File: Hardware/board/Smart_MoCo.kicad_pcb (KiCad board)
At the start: 4 copper layers, 26.9 x 39.9 mm, 37 parts, among them J1 Conn_01x02, J2 Conn_01x04, J3 Conn_01x02, J4 Conn_01x02, J5 Conn_01x04, J6 1722861102, J7 1722861102, U1 STM32F042F6Px, U2 VNH5019A-E, U3 SN65HVD232, U4 AP62200WU

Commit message: Reorganize Hardware folder and remove unused boards
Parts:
- H1, H2: footprint Local Libraries:Minimal_4_40_Hole -> Smart_MoCo:Minimal_4_40_Hole
- REF**: footprint Local Libraries:signature_Brendan_Westley -> Smart_MoCo:signature_Brendan_Westley

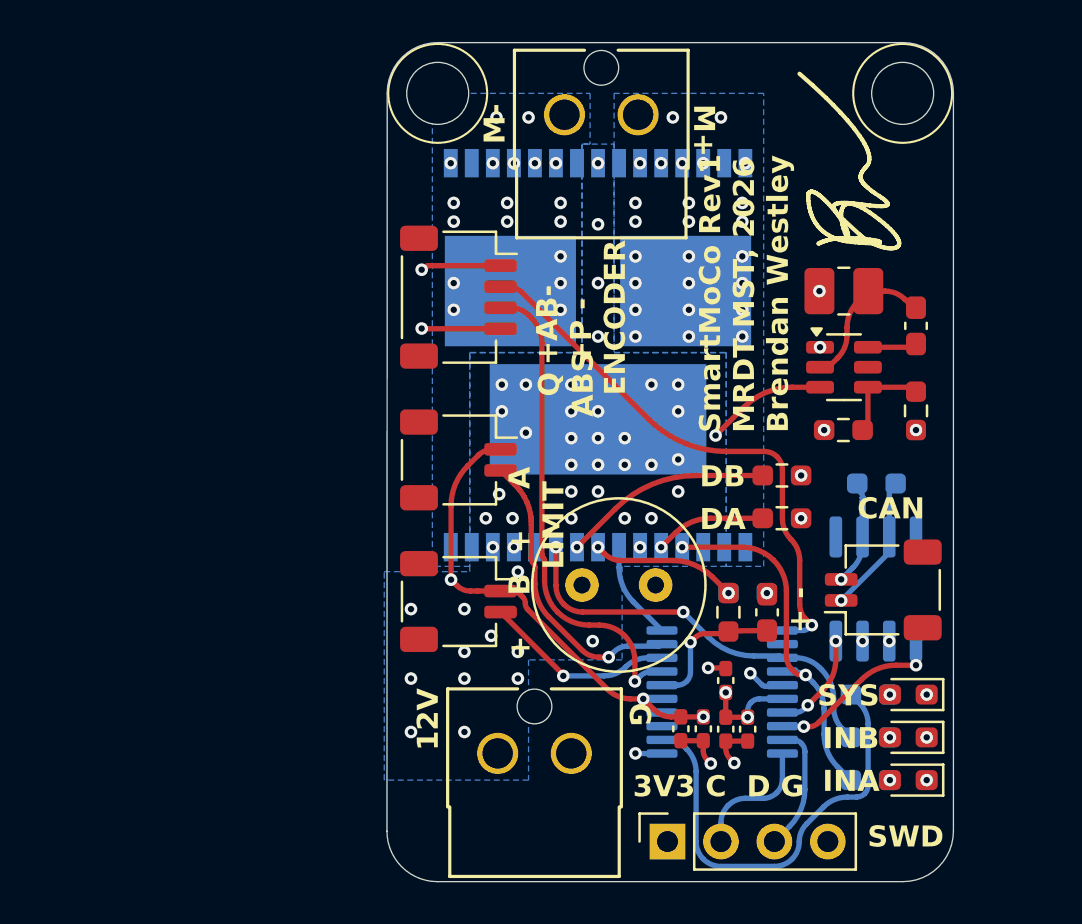
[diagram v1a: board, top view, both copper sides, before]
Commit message: Correct silkscreen labels
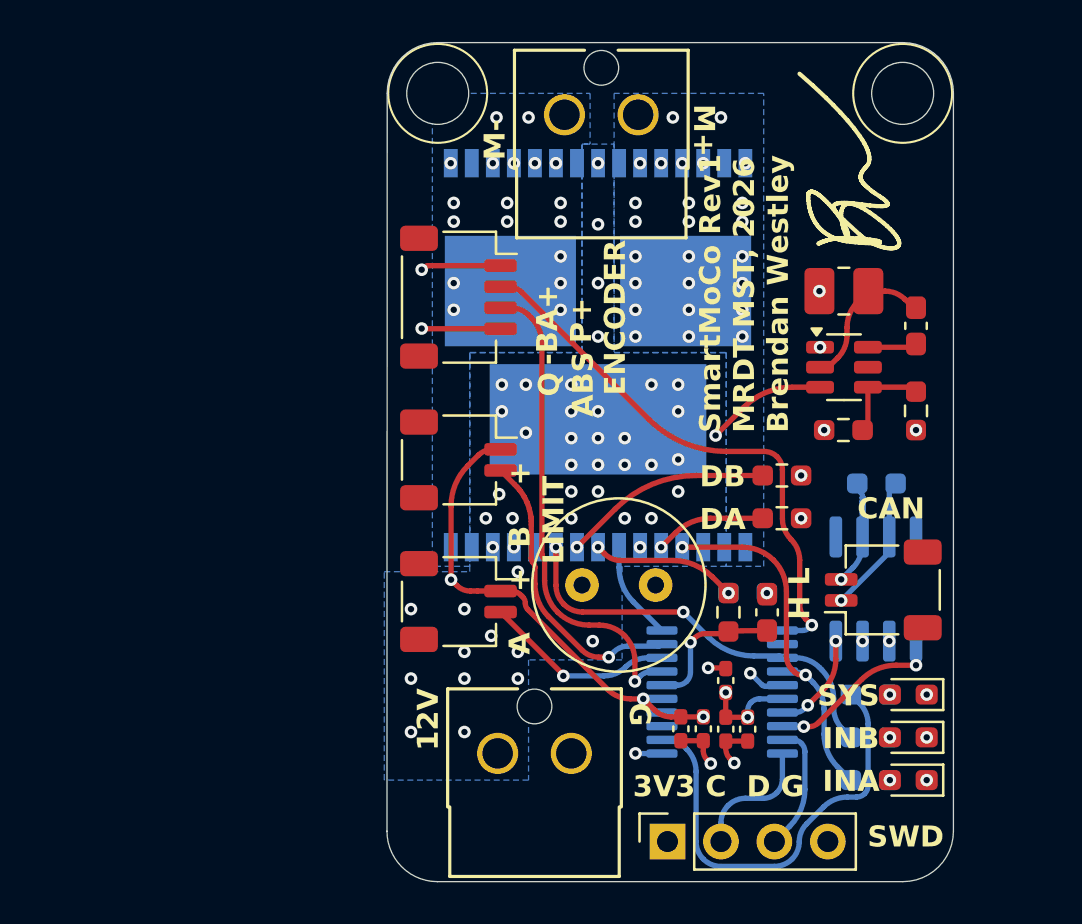
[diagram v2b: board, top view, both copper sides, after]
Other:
- board text added: "-BA+ - P+ ENCODER"
- board text added: "A + B + LIMIT"
- board text added: "H L"
- board text removed: "+ -"
- board text removed: "+ B + A LIMIT"
- board text removed: "+AB- +P - ENCODER"

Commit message: Redesign hardware
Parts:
- removed the J4 at (145.8, 78.5)
- removed J7: 1722861102, MRDT_Connectors:CONN_SD-172286-1000_02_MOL
- added C4: 22uF, Capacitor_SMD:C_0603_1608Metric_Pad1.08x0.95mm_HandSolder, B.Cu at (164.0, 76.1)
- added C5: 22uF, Capacitor_SMD:C_0603_1608Metric_Pad1.08x0.95mm_HandSolder, B.Cu at (162.5, 76.1)
- added J5: 1723103102, MRDT_Connectors:CONN_1723102000_02_MOL, F.Cu at (141.5, 83.0)
- added R10: 1k, Resistor_SMD:R_0603_1608Metric_Pad0.98x0.95mm_HandSolder, B.Cu at (141.0, 93.1)
- added R9: 1k, Resistor_SMD:R_0603_1608Metric_Pad0.98x0.95mm_HandSolder, B.Cu at (140.9, 90.5)
- C1, C3, L1, R1, R6, R7, U4: moved to B.Cu
- D1: value Red -> LED_RGBK; footprint LED_SMD:LED_0603_1608Metric_Pad1.05x0.95mm_HandSolder -> Smart_MoCo:PLCC4_3p5x2p8_SLD-L
- J1, J3: footprint Connector_JST:JST_SH_SM02B-SRSS-TB_1x02-1MP_P1.00mm_Horizontal -> Connector_JST:JST_XH_S2B-XH-A_1x02_P2.50mm_Horizontal
- J2: footprint Connector_JST:JST_SH_SM04B-SRSS-TB_1x04-1MP_P1.00mm_Horizontal -> Connector_JST:JST_XH_S4B-XH-A_1x04_P2.50mm_Horizontal
- J6: value 1722861102 -> 1723103102; footprint MRDT_Connectors:CONN_SD-172286-1000_02_MOL -> MRDT_Connectors:CONN_1723102000_02_MOL
- moved H1 46.0 mm to (133.9, 93.1)
- moved G*** 29.1 mm to (167.5, 67.0)
- moved D1 27.8 mm to (139.6, 93.3), turned to 0 degrees
- moved R8 27.4 mm to (138.0, 91.6), turned to -90 degrees
- moved D2 23.7 mm to (143.5, 93.1), turned to 90 degrees
- moved R12 21.8 mm to (143.5, 91.1), turned to -90 degrees
- moved D3 21.2 mm to (146.0, 93.1), turned to 90 degrees
- moved R11 19.5 mm to (146.0, 91.1), turned to -90 degrees
- moved J3 17.2 mm to (162.6, 81.5), turned to 90 degrees
- moved J2 16.9 mm to (162.5, 73.0), turned to 90 degrees
- moved J6 15.9 mm to (141.5, 71.5), turned to -90 degrees
- moved REF** 12.2 mm to (154.0, 71.0), turned to -90 degrees
- moved H2 11.5 mm to (133.9, 64.9)
- moved C1 10.6 mm to (150.5, 89.5), turned to 0 degrees
- moved R4 9.08 mm to (150.6, 86.5)
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- renumbered C8 to C10, C5 to C7, C4 to C8, C7 to C9, J5 to J4, R10 to R11, R9 to R12
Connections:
- D1 pad 1: GND -> Net-(D1-RA)
- D1 pad 2: Net-(D1-A) -> Net-(D1-GA)
- J3 pad 1: +3V3 -> LIM_A
- J3 pad 2: LIM_A -> LIM_B
- R8 pad 1: LED_STATUS -> LED_R
- R8 pad 2: Net-(D1-A) -> Net-(D1-RA)
- U1 pad 12: unconnected-(U1-PA6-Pad12) -> LED_R
- U1 pad 2: LED_STATUS -> LED_B
- U1 pad 3: unconnected-(U1-PF1-Pad3) -> LED_G
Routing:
- net LED_R: track 0.00 -> 24.2 mm, vias 0 -> 2
- net LED_STATUS: track 21.2 -> 0.00 mm
- net +3V3: track 31.3 -> 16.1 mm, vias 11 -> 6
- net LED_G: track 0.00 -> 14.1 mm
- net LED_B: track 0.00 -> 13.4 mm
- net Net-(U2-EN/DIAGB): track 9.98 -> 1.83 mm
- net ENC_A/PWM: track 26.1 -> 19.3 mm
- net IN_B: track 19.7 -> 24.9 mm, vias 2 -> 3
- net ENC_B: track 23.1 -> 27.8 mm, vias 1 -> 0
- net CS: track 6.95 -> 3.28 mm, vias 1 -> 0
- net Net-(U2-EN/DIAGA): track 5.28 -> 1.76 mm
- net LIM_A: track 9.17 -> 12.4 mm, vias 1 -> 0
- net SWCLK: track 6.51 -> 9.34 mm
- net IN_A: track 17.5 -> 20.2 mm, vias 2 -> 3
- net +12V: track 5.76 -> 8.43 mm, vias 46 -> 15
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- removed copper zone on In2.Cu, net /OUTB
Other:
- board size 26.9 x 39.9 mm -> 40.5 x 33 mm
- board text added: "3V3 C D G SWD"
- board text added: "B A LIMIT"
- board text added: "G B A 3V3 ENCODER"
- board text added: "L H CAN"
- board text added: "SmartMoCo Rev2 MRDT MST, 2026 Brendan Westley"
- board text removed: "-BA+ - P+ ENCODER"
- board text removed: "3V3 C D G"
- board text removed: "A + B + LIMIT"
- board text removed: "CAN"
- board text removed: "H L"
- board text removed: "Q ABS"
- board text removed: "SWD"
- board text removed: "SmartMoCo Rev1 MRDT MST, 2026 Brendan Westley"

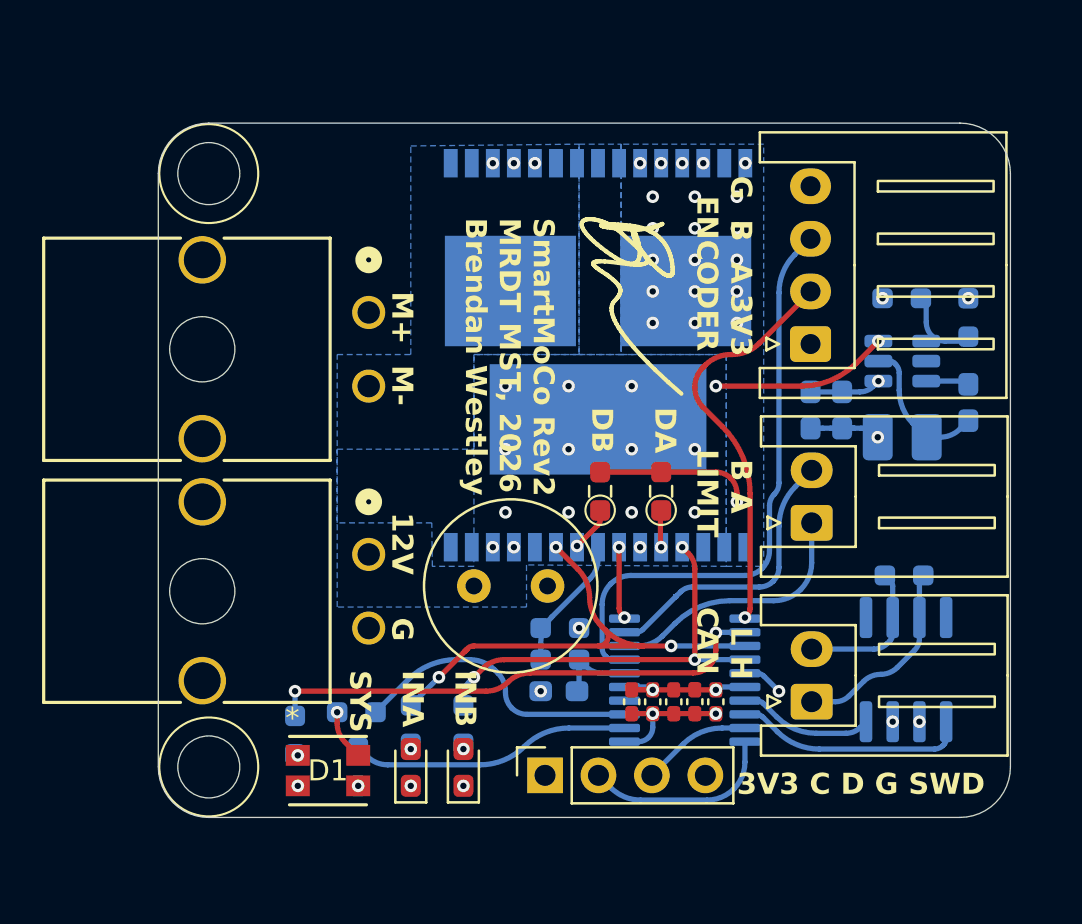
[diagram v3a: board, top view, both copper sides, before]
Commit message: Incorporate review 1 feedback
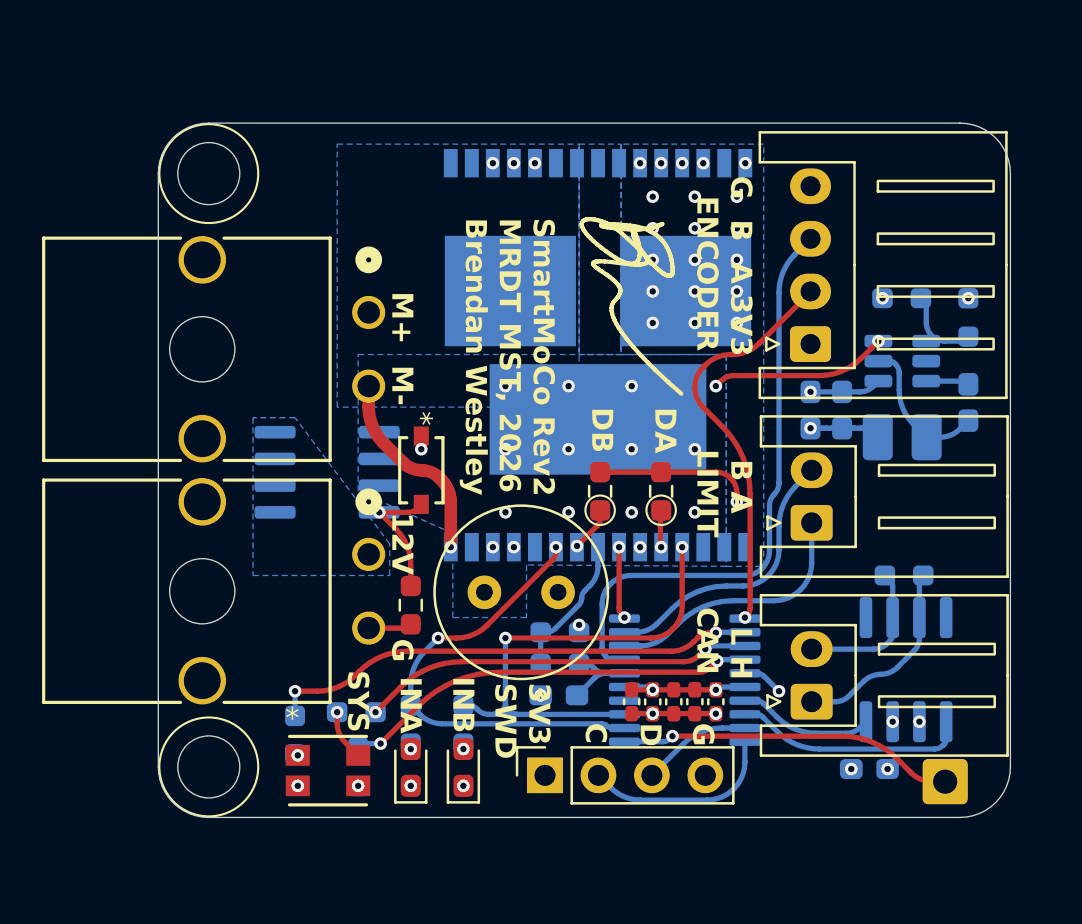
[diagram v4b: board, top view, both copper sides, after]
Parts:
- added C11: 100nF, Capacitor_SMD:C_0603_1608Metric_Pad1.08x0.95mm_HandSolder, B.Cu at (165.3, 93.2)
- added D4: MMSZ5240BT1G, MRDT_Devices:SOD-123_ONS-L, F.Cu at (144.0, 79.0)
- added J7: Conn_01x01, Connector_Wire:SolderWire-0.5sqmm_1x01_D0.9mm_OD2.1mm, B.Cu at (168.9, 93.8)
- added R13: 10k, Resistor_SMD:R_0603_1608Metric_Pad0.98x0.95mm_HandSolder, F.Cu at (143.5, 85.4)
- added U5: TPC8132_LQS, Package_SO:SOIC-8_3.9x4.9mm_P1.27mm, B.Cu at (139.5, 79.1)
- J5, J6: value 1723103102 -> Molex_UltraFit_02
- moved C2 0.58 mm to (147.0, 84.8)
- moved C1 0.20 mm to (150.5, 89.7)
- moved R1 0.20 mm to (150.6, 88.2)
- moved R4 0.20 mm to (150.6, 86.7)
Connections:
- J5 pad 1: +12V -> Net-(U5-D)
- U1 pad 1: GND -> GPIO
- U1 pad 13: IN_B -> LED_G
- U1 pad 14: IN_A -> LED_B
- U1 pad 2: LED_B -> IN_B
- U1 pad 3: LED_G -> IN_A
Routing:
- net GPIO: track 0.00 -> 16.0 mm, vias 0 -> 1
- net /OUTB: track 0.00 -> 9.55 mm, vias 0 -> 1
- net LED_B: track 13.4 -> 19.8 mm, vias 0 -> 2
- net Net-(U5-G): track 0.00 -> 6.13 mm, vias 0 -> 1
- net LED_G: track 14.1 -> 18.6 mm, vias 0 -> 2
- net IN_A: track 20.2 -> 24.6 mm, vias 3 -> 2
- net IN_B: track 24.9 -> 21.6 mm, vias 3 -> 2
- net CS: track 3.28 -> 4.53 mm
- net LED_R: track 24.2 -> 23.3 mm
- net GND: track 11.3 -> 11.0 mm, vias 18 -> 19
- net +3V3: vias 6 -> 7
- net +12V: vias 15 -> 16
- added copper zone on B.Cu, net Net-(U5-D)
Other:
- board text added: "3V3 SWD"
- board text added: "C"
- board text added: "D"
- board text removed: "3V3 C D G SWD"

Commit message: Incorporate review 2 feedback
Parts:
- J5, J6: value Molex_UltraFit_02 -> Molex_UltraFit_02_Horizontal; footprint MRDT_Connectors:CONN_1723102000_02_MOL -> MRDT_Connectors:MOLEX_UltraFit_02_Horizontal
- moved H1 1.40 mm to (132.5, 93.1)
- moved H2 1.40 mm to (132.5, 64.9)
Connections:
- J5 pad MP: (no net) -> GND
- J6 pad MP: (no net) -> GND
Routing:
- net GND: track 11.0 -> 9.95 mm
- net +3V3: track 16.1 -> 15.2 mm
- net IN_A: track 24.6 -> 23.9 mm
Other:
- board size 40.5 x 33 mm -> 41.9 x 33 mm
